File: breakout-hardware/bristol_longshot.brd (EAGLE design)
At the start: 12 x 30 mm, 66 parts, among them U3 74LVC1G04GW

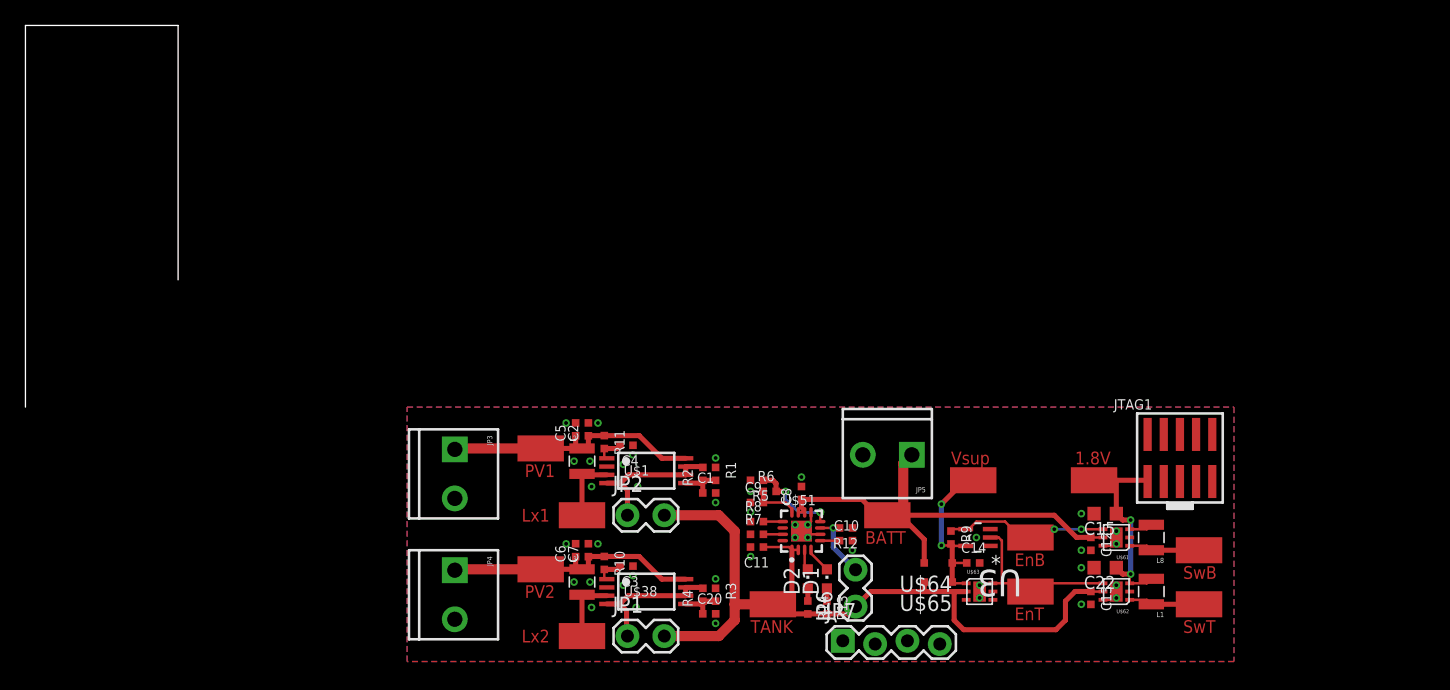
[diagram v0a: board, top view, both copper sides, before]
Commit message: Added note about Ct on supervisor
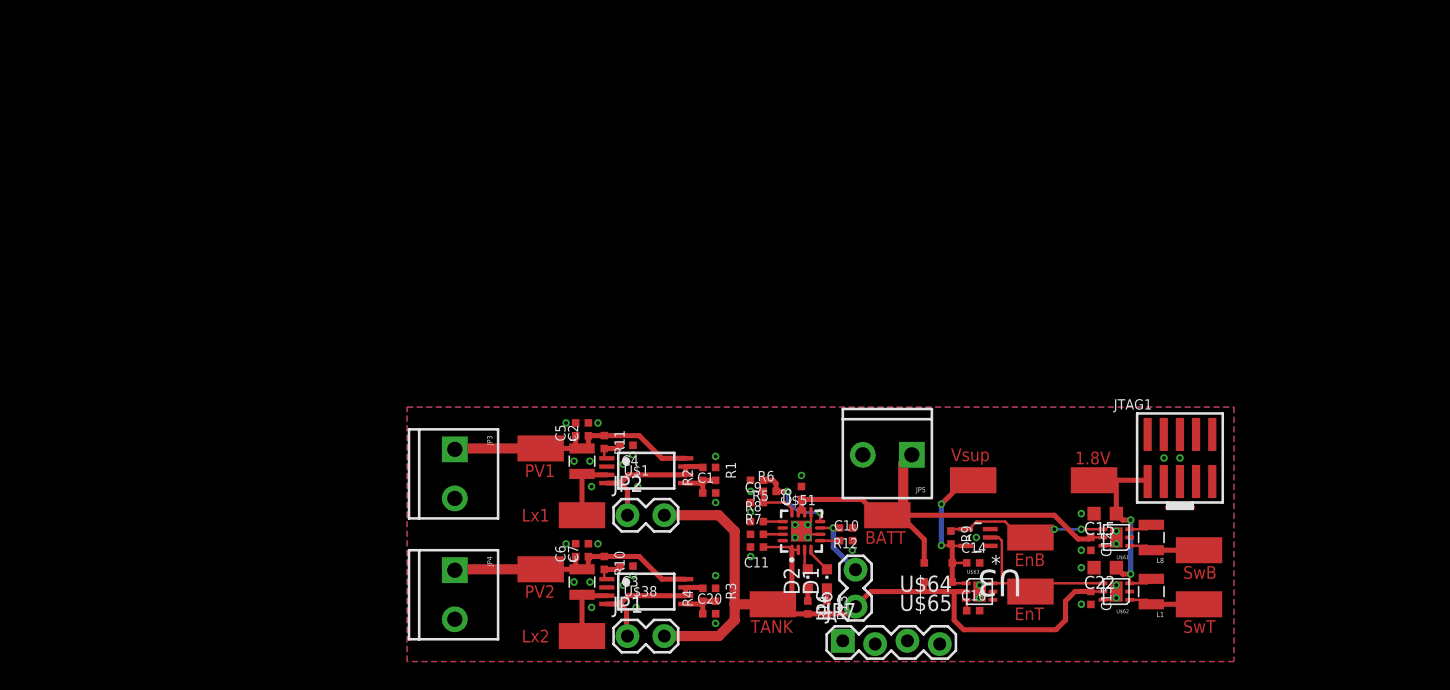
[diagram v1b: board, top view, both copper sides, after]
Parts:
- added C16: DNP, microbuilder_v3:_0402
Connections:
- new net N$2: C16.1, U$63.3
- net GND: now also C16.2
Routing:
- net N$4: track 0.00 -> 2.00 mm
- net N$2: track 0.00 -> 0.89 mm
- net TH: track 7.00 -> 7.04 mm, vias 3 -> 2
- net GND: vias 40 -> 42
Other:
- board outline removed
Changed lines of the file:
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@@
 <setting verticaltext="up"/>
 </settings>
-<grid distance="1" unitdist="mm" unit="mm" style="lines" multiple="1" display="yes" altdistance="0.025" altunitdist="inch" altunit="inch"/>
+<grid distance="0.125" unitdist="mm" unit="mm" style="lines" multiple="1" display="yes" altdistance="0.025" altunitdist="inch" altunit="inch"/>
 <layers>
 <layer number="1" name="Top" color="4" fill="1" visible="yes" active="yes"/>
@@
 <board>
 <plain>
-<wire x1="-30" y1="20" x2="-30" y2="50" width="0" layer="20"/>
-<wire x1="-30" y1="50" x2="-18" y2="50" width="0" layer="20"/>
-<wire x1="-18" y1="50" x2="-18" y2="30" width="0" layer="20"/>
 <text x="61" y="6.5" size="1" layer="1" font="vector" ratio="16">SwB</text>
 <text x="61" y="2.25" size="1" layer="1" font="vector" ratio="16">SwT</text>
@@
 <text x="36" y="9.25" size="1" layer="1" font="vector" ratio="16">BATT</text>
 <text x="52.5" y="15.5" size="1" layer="1" font="vector" ratio="16">1.8V</text>
-<text x="42.75" y="15.5" size="1" layer="1" font="vector" ratio="16">Vsup</text>
+<text x="42.75" y="15.75" size="1" layer="1" font="vector" ratio="16">Vsup</text>
 <text x="9.25" y="14.5" size="1" layer="1" font="vector" ratio="16">PV1</text>
 <text x="9.25" y="5" size="1" layer="1" font="vector" ratio="16">PV2</text>
@@
 <element name="JP7" library="SparkFun" package="1X04_LOCK" value="" x="34.25" y="1.5"/>
 <element name="C15" library="resistor" package="C0603K" value="10µF" x="54.875" y="11.625" rot="R180"/>
+<element name="C16" library="microbuilder_v3" package="_0402" value="DNP" x="44.5" y="4"/>
 </elements>
 <signals>
@@
 <via x="15" y="9.25" extent="1-16" drill="0.3"/>
 <via x="17" y="6" extent="1-16" drill="0.3"/>
-<via x="24.25" y="6.5" extent="1-16" drill="0.3"/>
+<via x="24.25" y="6.75" extent="1-16" drill="0.3"/>
 <via x="24.25" y="3" extent="1-16" drill="0.3"/>
 <via x="17.75" y="16.25" extent="1-16" drill="0.3"/>
 <via x="17" y="15.5" extent="1-16" drill="0.3"/>
 <via x="24.25" y="12.5" extent="1-16" drill="0.3"/>
-<via x="24.25" y="16" extent="1-16" drill="0.3"/>
+<via x="24.25" y="16.125" extent="1-16" drill="0.3"/>
 <via x="12.5" y="18.75" extent="1-16" drill="0.3"/>
 <via x="15" y="18.75" extent="1-16" drill="0.3"/>
@@
 <contactref element="JP7" pad="4"/>
 <contactref element="R12" pad="1"/>
-<via x="31" y="14.5" extent="1-16" drill="0.3"/>
+<via x="31" y="14.625" extent="1-16" drill="0.3"/>
 <via x="30.5" y="10.75" extent="1-16" drill="0.3"/>
 <via x="30.5" y="9.75" extent="1-16" drill="0.3"/>
@@
 <via x="18" y="4.25" extent="1-16" drill="0.3"/>
 <via x="14.5" y="4.25" extent="1-16" drill="0.3"/>
+<contactref element="C16" pad="2"/>
+<via x="59.5" y="16" extent="1-16" drill="0.3"/>
+<via x="60.75" y="16" extent="1-16" drill="0.3"/>
 </signal>
 <signal name="KEY">
@@
 <wire x1="30.75" y1="11.725" x2="31.25" y2="11.725" width="0.2" layer="1"/>
 <wire x1="31.25" y1="11.725" x2="31" y2="11.975" width="0.2" layer="1"/>
-<wire x1="31" y1="11.975" x2="31" y2="12.742" width="0.4" layer="1" style="longdash"/>
+<wire x1="31" y1="11.975" x2="31" y2="12.742" width="0.4" layer="1"/>
 <wire x1="37.75" y1="11.5" x2="37" y2="11.5" width="0.4" layer="1"/>
 <wire x1="37" y1="11.5" x2="35.758" y2="12.742" width="0.4" layer="1"/>
@@
 <wire x1="40.65" y1="7.75" x2="40.65" y2="9.6" width="0.4" layer="1"/>
 <wire x1="40.65" y1="9.6" x2="38.625" y2="11.625" width="0.4" layer="1"/>
-<wire x1="53.75" y1="9.758" x2="52.617" y2="9.758" width="0.4" layer="1"/>
-<wire x1="52.617" y1="9.758" x2="50.875" y2="11.5" width="0.4" layer="1"/>
+<wire x1="52.742" y1="9.633" x2="50.875" y2="11.5" width="0.4" layer="1"/>
 <wire x1="50.875" y1="11.5" x2="37.75" y2="11.5" width="0.4" layer="1"/>
+<wire x1="52.742" y1="9.633" x2="53.625" y2="9.633" width="0.4" layer="1"/>
+<wire x1="53.625" y1="9.633" x2="53.75" y2="9.758" width="0.4" layer="1"/>
 </signal>
 <signal name="LX1">
@@
 <contactref element="R5" pad="1"/>
 <contactref element="U$51" pad="P$8"/>
-<via x="32.5" y="11.75" extent="1-16" drill="0.3"/>
 <wire x1="32.475" y1="11" x2="32.475" y2="11.725" width="0.2" layer="1"/>
-<wire x1="32.475" y1="11.725" x2="32.5" y2="11.75" width="0.2" layer="1"/>
 <wire x1="28.008" y1="14.25" x2="28.75" y2="14.25" width="0.4" layer="1"/>
 <wire x1="28.75" y1="14.25" x2="29" y2="14" width="0.4" layer="1"/>
 <wire x1="29" y1="14" x2="29" y2="13.383" width="0.4" layer="1"/>
 <wire x1="29" y1="13.383" x2="29.008" y2="13.375" width="0.4" layer="1"/>
-<via x="29.75" y="13.375" extent="1-16" drill="0.3"/>
-<wire x1="29.008" y1="13.375" x2="29.75" y2="13.375" width="0.4" layer="1"/>
+<via x="29.875" y="13.375" extent="1-16" drill="0.3"/>
+<wire x1="29.008" y1="13.375" x2="29.875" y2="13.375" width="0.4" layer="1"/>
 <via x="32.475" y="11.725" extent="1-16" drill="0.3"/>
 <wire x1="32.475" y1="11.725" x2="30.775" y2="11.725" width="0.2" layer="16"/>
-<wire x1="30.775" y1="11.725" x2="29.75" y2="12.75" width="0.2" layer="16"/>
-<wire x1="29.75" y1="12.75" x2="29.75" y2="13.375" width="0.2" layer="16"/>
+<wire x1="30.775" y1="11.725" x2="29.875" y2="12.625" width="0.2" layer="16"/>
+<wire x1="29.875" y1="12.625" x2="29.875" y2="13.375" width="0.2" layer="16"/>
 </signal>
 <signal name="VREF">
@@
 <wire x1="31.25" y1="7.5" x2="31.5" y2="7.25" width="0.2" layer="1"/>
 </signal>
+<signal name="N$2">
+<contactref element="U$63" pad="3"/>
+<contactref element="C16" pad="1"/>
+<wire x1="43.95" y1="4.85" x2="43.992" y2="4.85" width="0.2" layer="1"/>
+<wire x1="43.992" y1="4.85" x2="43.992" y2="4" width="0.2" layer="1"/>
+</signal>
+<signal name="N$4">
+<wire x1="59.75" y1="12.125" x2="61.75" y2="12.125" width="0.4" layer="1"/>
+</signal>
 </signals>
+<errors>
+</errors>
 </board>
 </drawing>

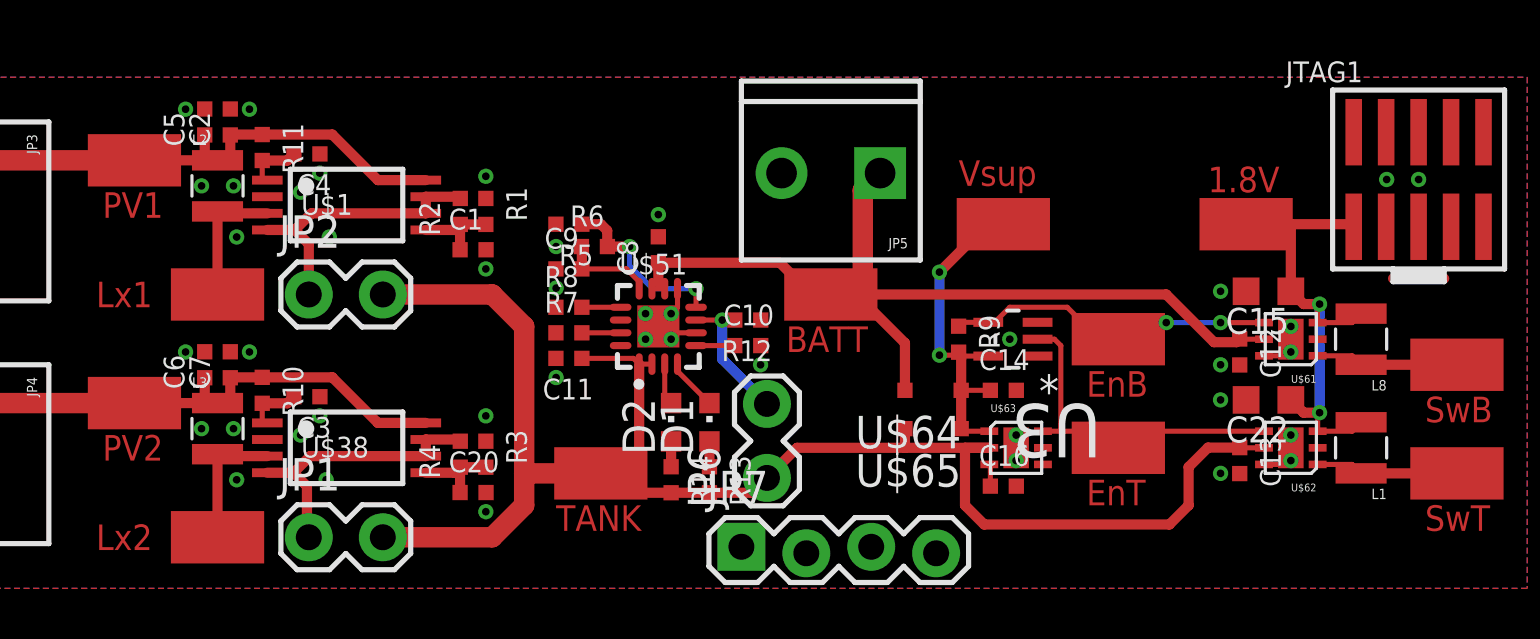
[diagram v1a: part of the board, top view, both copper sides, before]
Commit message: Added pdf of breakout
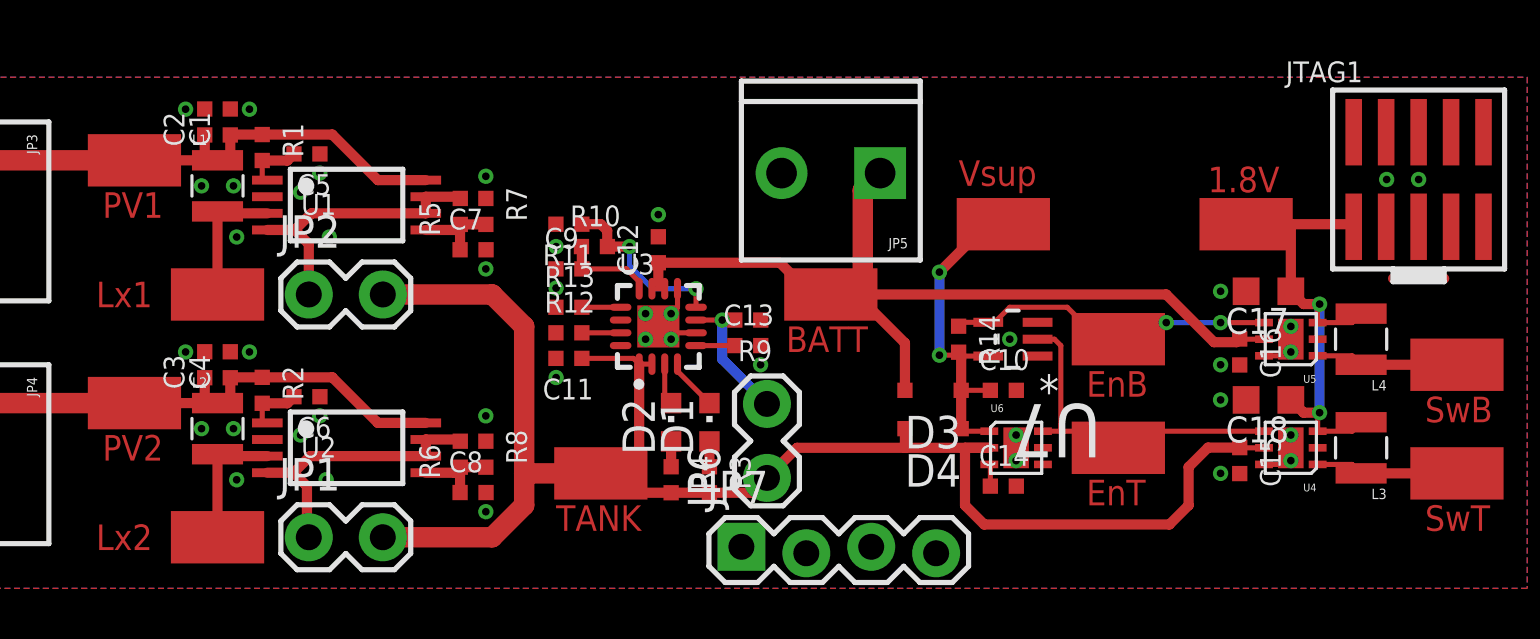
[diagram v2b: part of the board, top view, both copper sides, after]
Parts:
- removed C20: 1nF, microbuilder_v3:_0402
- removed U$51: L6924D, l6924d:VFQFPN16
- added C17: 10µF, resistor:C0603K
- added U7: 74LVC1G04GW, 74LVC1G04GW_inverter:SOT65P210X110-5N
- C1, C3, C4: value 1nF -> 4.7µF
- C10: value 47nF -> 1nF
- C13: value 4.7µF -> 47nF
- C14: value 1nF -> DNP
- C15: value 10µF -> 4.7µF; device resistor:C0603K -> microbuilder_v3:_0402
- C16: value DNP -> 4.7µF
- C5, C6, C7, C8: value 4.7µF -> 1nF
- R1, R3: value 820kΩ -> 1kΩ
- R10: value 1kΩ -> 100kΩ
- R11: value 1kΩ -> 47kΩ
- R12: value 100kΩ -> 47kΩ
- R13, R14: value 1kΩ -> 10kΩ
- R2, R4: value 2M2Ω -> 1kΩ
- R5: value 47kΩ -> 2M2Ω
- R6: value 100kΩ -> 2M2Ω
- R7: value 47kΩ -> 820kΩ
- R8: value 10kΩ -> 820kΩ
- R9: value 10kΩ -> 100kΩ
- U3: value 74LVC1G04GW -> L6924D; device 74LVC1G04GW_inverter:SOT65P210X110-5N -> l6924d:VFQFPN16
- moved L1 45.9 mm to (13.8, 15.8), turned to 0 degrees
- moved L3 44.8 mm to (58.5, 5.50), turned to 180 degrees
- moved C12 23.1 mm to (31.0, 13.2), turned to 90 degrees
- moved C13 19.8 mm to (34.5, 9.50), turned to 0 degrees
- moved R10 14.2 mm to (28.5, 13.4), turned to 0 degrees
- moved U3 13.9 mm to (31.0, 10.2), turned to 0 degrees
- moved R14 12.5 mm to (42.8, 9.75)
- moved R11 12.4 mm to (27.5, 14.2), turned to 180 degrees
- moved C8 12.0 mm to (23.8, 3.75), turned to 0 degrees
- moved C1 10.7 mm to (14.2, 18.2), turned to 90 degrees
- moved C16 10.6 mm to (53.8, 9.25), turned to 270 degrees
- moved C7 10.5 mm to (23.8, 13.2), turned to 0 degrees
- moved R2 10.4 mm to (15.5, 7.75), turned to 270 degrees
- moved C10 10.2 mm to (44.5, 7.75)
- moved R6 9.67 mm to (23.2, 5.25), turned to 90 degrees
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- renumbered C22 to C18, L8 to L4, U$1 to U1, U$38 to U2, U$61 to U5, U$62 to U4, U$63 to U6, U$64 to D3, U$65 to D4
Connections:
- net 1.8V: now also C17.1, L3.2; no longer C15.1, L1.2
- net BATTERY: now also C16.1, U3.P$10, U3.P$11; no longer C8.1, U$51.P$10, U$51.P$11
- net BATTERY_EN: now also R14.1, U7.4; no longer R9.1, U3.4
- net GND: now also C17.2, C3.2, C4.2, C5.1, C6.1, R11.2, R13.1, R9.1, U3.P$17, U3.P$6, U3.P$9, U7.3; no longer C20.2, C3.1, C4.1, C5.2, C6.2, R1.1, R3.1, R5.2, U$51.P$17, U$51.P$6, U$51.P$9, U3.3
- net IPRE: now also U3.P$16; no longer U$51.P$16
- net LX1: now also L1.2; no longer L2.2
- net LX2: now also L2.2; no longer L3.2
- net MPP-SET2: now also C6.2, R2.2; no longer C3.2, R10.2
- net MPPT-VOUT-1: now also R5.2; no longer R2.2
- net MPPT-VOUT-2: now also R6.2; no longer R4.2
- net N$1: now also C5.2, R1.2; no longer C4.2, R11.2
- net N$2: now also C14.1; no longer C16.1
- net N$3: now also C13.1, U3.P$5; no longer C10.1, U$51.P$5
- net N$6: now also R3.1; no longer R13.1
- net N$8: now also R4.1; no longer R14.1
- net PV1: now also C1.1, L1.1, R1.1; no longer C5.1, L2.1, R11.1
- net PV2: now also C3.1, C4.1, L2.1, R2.1; no longer C6.1, C7.1, L3.1, R10.1
- net REND: now also R13.2, U3.P$13; no longer R8.2, U$51.P$13
- net RPRG: now also R12.2, U3.P$15; no longer R7.2, U$51.P$15
- net SD: now also R9.2, U3.P$7; no longer R12.2, U$51.P$7
- net SPV_VCTRL1: now also C7.1, R5.1, R7.2; no longer C1.1, R1.2, R2.1
- net SPV_VCTRL2: now also C8.1, R6.1, R8.2; no longer C20.1, R3.2, R4.1
- net ST1: now also U3.P$4; no longer U$51.P$4
- net ST2: now also U3.P$3; no longer U$51.P$3
- net SUPERVISOR_VCC: now also C10.1, R14.2, U7.5; no longer C14.1, R9.2, U3.5
- net TANK: now also C15.1, R3.2, R4.2, U3.P$1, U3.P$2; no longer C13.1, R13.2, R14.2, U$51.P$1, U$51.P$2
- net TANK_BUCK_SW: now also L3.1; no longer L1.1
- net TANK_EN: now also U7.2; no longer U3.2
- net TH: now also R10.2, R11.1, U3.P$8; no longer R5.1, R6.2, U$51.P$8
- net VPRE: now also U3.P$14; no longer U$51.P$14
- net VREF: now also R10.1, U3.P$12; no longer R6.1, U$51.P$12
